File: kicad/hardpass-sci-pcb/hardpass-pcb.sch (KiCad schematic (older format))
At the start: 45 parts, among them IC1 APX803, P1 Pi_Zero, P2 OLED_I2C, P3 Pi_Zero, SW1 1, SW10 C/UP, SW11 0/OK, SW12 OK/DN, SW13 SHUTDN, SW2 2, SW3 3, SW4 4, SW5 5, SW6 6, SW7 7, SW8 8, SW9 9, U1 ISO7816, U2 ESP-12E, U3 SEC1210

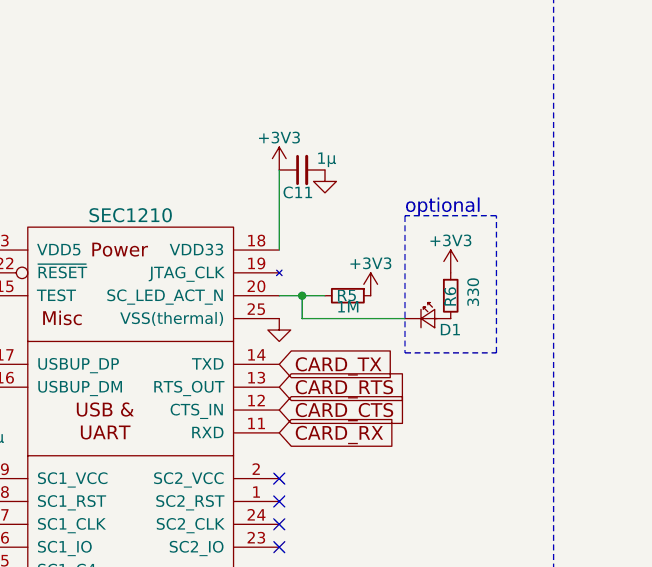
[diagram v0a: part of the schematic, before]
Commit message: small fixes
schematic: add either-or text to card-led
pcb: connect c10 to card-pin1
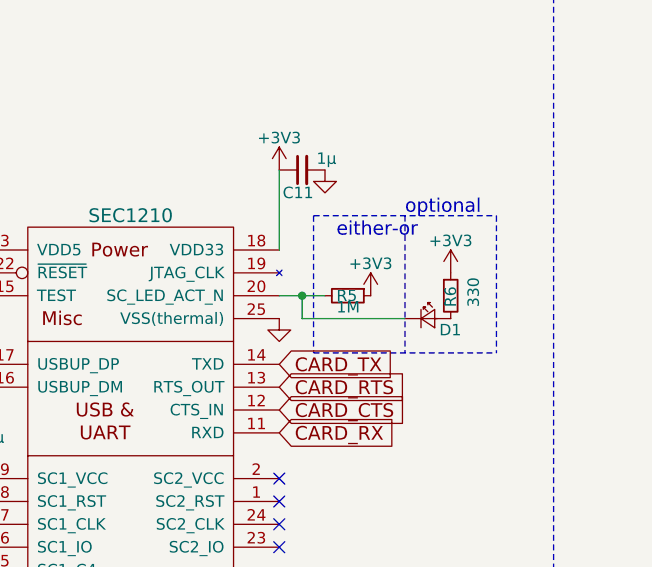
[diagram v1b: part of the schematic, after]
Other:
- note added: "either-or"
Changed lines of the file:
@@
 	10500 1600 10500 2200
 Wire Notes Line
-	10500 2200 10900 2200
+	10100 2200 10900 2200
 Wire Notes Line
-	10900 2200 10900 1600
+	10900 1600 10900 2200
 Wire Notes Line
-	10900 1600 10500 1600
+	10100 1600 10900 1600
 Text Notes 10500 1600 0    60   ~ 0
 optional
@@
 Text Notes 9300 3950 0    60   ~ 0
 CTS/RTS on the Pi: \nhttps://github.com/mholling/rpirtscts
+Wire Notes Line
+	10100 1600 10100 2200
+Text Notes 10200 1700 0    60   ~ 0
+either-or
 $EndSCHEMATC

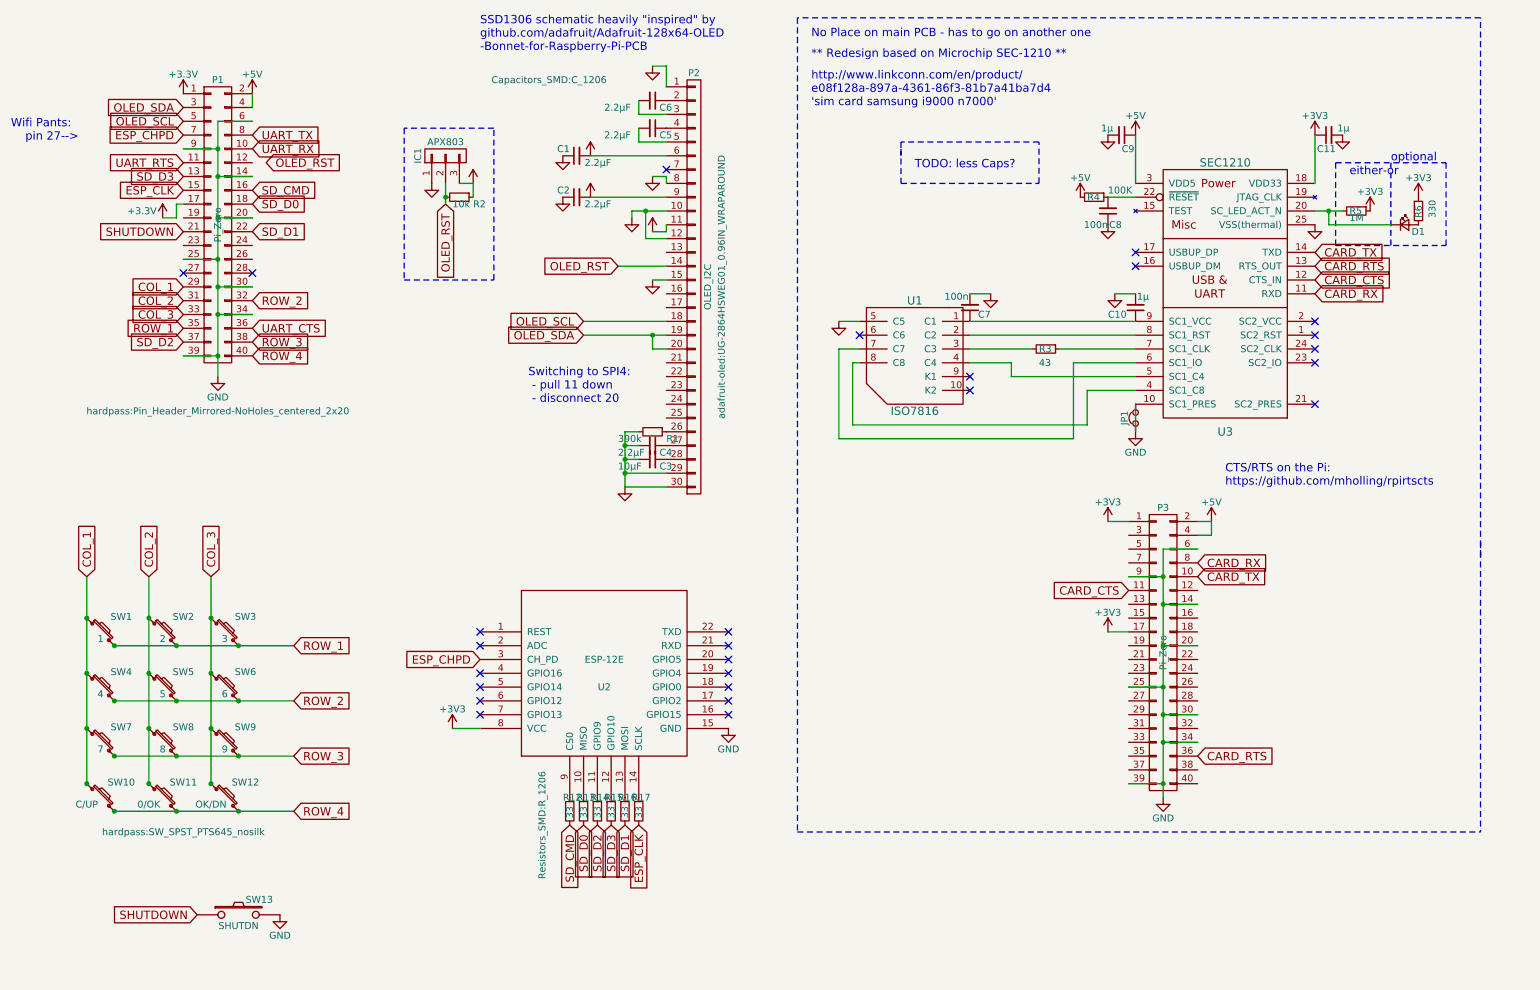
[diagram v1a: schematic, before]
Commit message: seperate hardpass and hardpass-sci kicad projects
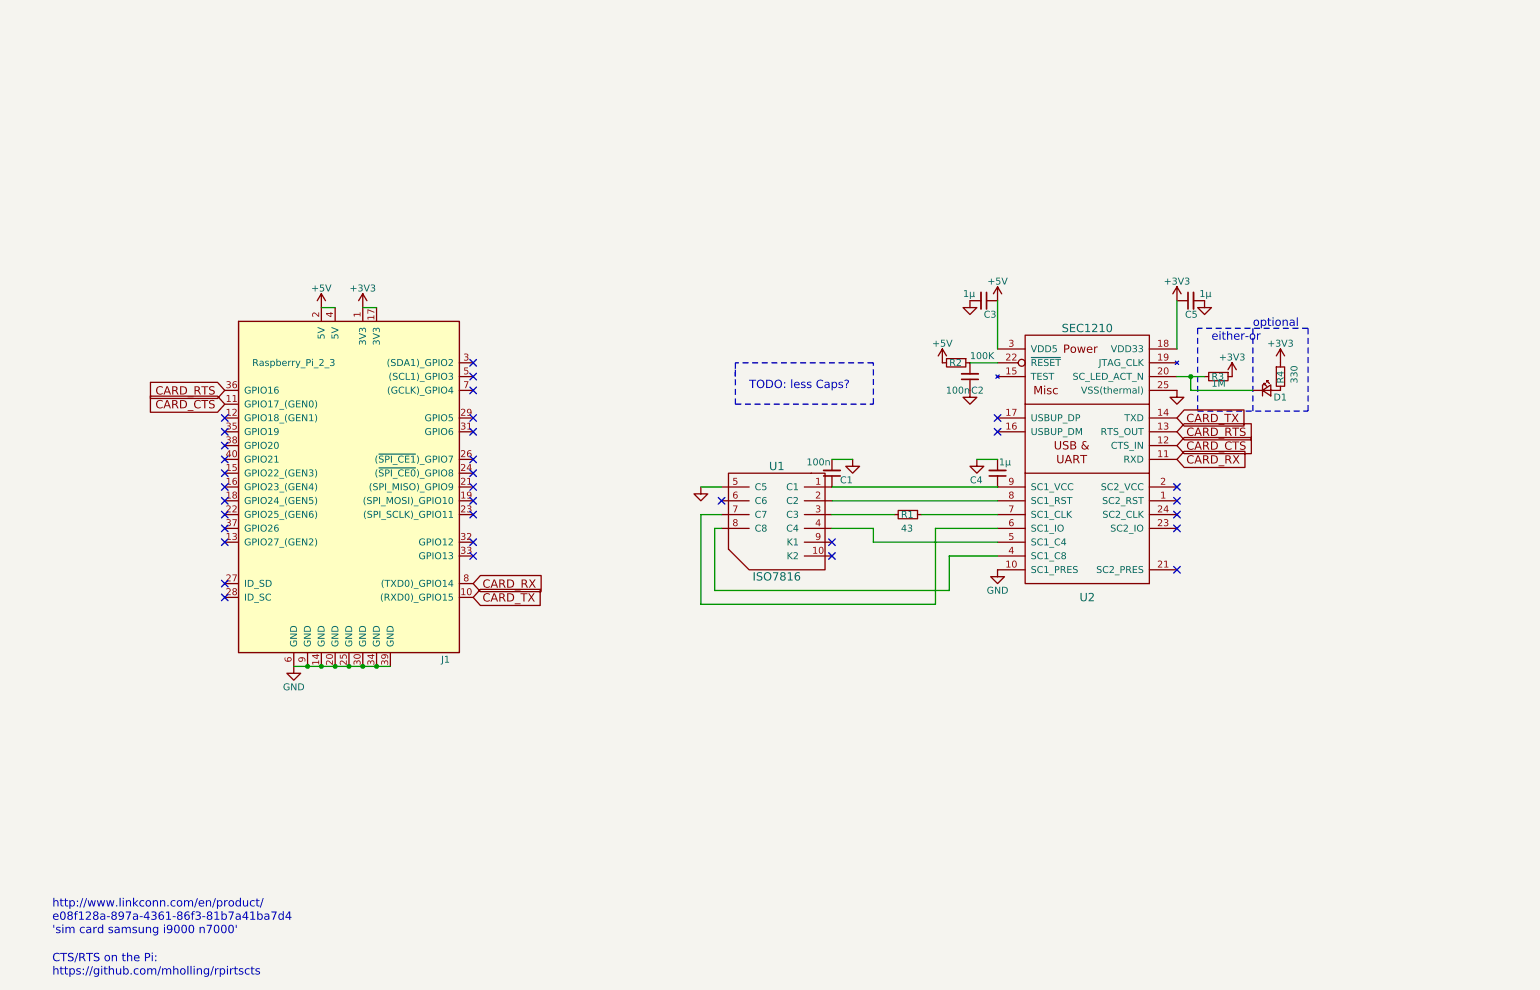
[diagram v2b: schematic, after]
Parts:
- removed C1, C2, C4, C5, C6: 2.2µF, Capacitors_SMD:C_1206, symbol C_Small
- removed C3: 10µF, Capacitors_SMD:C_1206, symbol C_Small
- removed IC1: APX803, TO_SOT_Packages_SMD:SOT-23, symbol CONN_01X03
- removed JP1: (no value), Resistors_SMD:R_0603, symbol Jumper_NC_Small
- removed P1: Pi_Zero, hardpass:Pin_Header_Mirrored-NoHoles_centered_2x20, symbol CONN_02X20
- removed P2: OLED_I2C, adafruit-oled:UG-2864HSWEG01_0.96IN_WRAPAROUND, symbol CONN_01X30
- removed P3: Pi_Zero, hardpass:Pin_Header_Straight_2x20_Pitch2.54mm_centered, symbol CONN_02X20
- removed R1: 390k, Resistors_SMD:R_1206, symbol R_Small
- removed R12, R13, R14, R15, R16, R17: 33, Resistors_SMD:R_1206, symbol R_Small
- removed R2: 10k, Resistors_SMD:R_1206, symbol R_Small
- removed SW1: 1, hardpass:SW_SPST_PTS645_nosilk, symbol SW_PUSH_SMALL
- removed SW10: C/UP, hardpass:SW_SPST_PTS645_nosilk, symbol SW_PUSH_SMALL
- removed SW11: 0/OK, hardpass:SW_SPST_PTS645_nosilk, symbol SW_PUSH_SMALL
- removed SW12: OK/DN, hardpass:SW_SPST_PTS645_nosilk, symbol SW_PUSH_SMALL
- removed SW13: SHUTDN, symbol SW_PUSH
- removed SW2: 2, hardpass:SW_SPST_PTS645_nosilk, symbol SW_PUSH_SMALL
- removed SW3: 3, hardpass:SW_SPST_PTS645_nosilk, symbol SW_PUSH_SMALL
- removed SW4: 4, hardpass:SW_SPST_PTS645_nosilk, symbol SW_PUSH_SMALL
- removed SW5: 5, hardpass:SW_SPST_PTS645_nosilk, symbol SW_PUSH_SMALL
- removed SW6: 6, hardpass:SW_SPST_PTS645_nosilk, symbol SW_PUSH_SMALL
- removed SW7: 7, hardpass:SW_SPST_PTS645_nosilk, symbol SW_PUSH_SMALL
- removed SW8: 8, hardpass:SW_SPST_PTS645_nosilk, symbol SW_PUSH_SMALL
- removed SW9: 9, hardpass:SW_SPST_PTS645_nosilk, symbol SW_PUSH_SMALL
- removed U2: ESP-12E, hardpass:ESP-12E_smd, symbol ESP-12E
- added J1: Raspberry_Pi_2_3, Pin_Headers:Pin_Header_Straight_2x20, symbol Raspberry_Pi_2_3
- renumbered C7 to C1, C8 to C2, C9 to C3, C10 to C4, C11 to C5, R3 to R1, R4 to R2, R5 to R3, R6 to R4, U3 to U2
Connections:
- net +3V3: now also J1.1 (3V3), J1.17 (3V3)
- net +5V: now also J1.2 (5V), J1.4 (5V)
- net CARD_CTS: now also J1.11 (GPIO17_(GEN0))
- net CARD_RTS: now also J1.36 (GPIO16)
- net CARD_RX: now also J1.8 ((TXD0)_GPIO14)
- net CARD_TX: now also J1.10 ((RXD0)_GPIO15)
- net GND: now also J1.14 (GND), J1.20 (GND), J1.25 (GND), J1.30 (GND), J1.34 (GND), J1.39 (GND), J1.6 (GND), J1.9 (GND)
- no-connect marks 26 -> 34
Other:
- note removed: "** Redesign based on Microchip SEC-1210 **"
- note removed: "No Place on main PCB - has to go on another one"
- note removed: "SSD1306 schematic heavily "inspired" by\ngithub.com/adafruit/Adafruit-128x64-OLED\n-Bonnet-for-Raspberry-Pi-PCB"
- note removed: "Switching to SPI4:\n - pull 11 down\n - disconnect 20"
- note removed: "Wifi Pants: \n pin 27-->"
- moved on the sheet: C1, C2, C3, C4, C5, D1, R1, R2, R3, R4, U1, U2

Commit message: change sec1210 footprint to handsoldering
should ease qfn soldering by hand due to the elongated pads. this also
required moveing some traces out of the way on the pcb.
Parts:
- U2: footprint Housings_DFN_QFN:QFN-24-1EP_5x5mm_Pitch0.65mm -> Housings_DFN_QFN:QFN-24-1EP_5x5mm_Pitch0.65mm_HandSoldering
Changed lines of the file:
@@
 F 0 "U2" H 8300 2750 60  0000 C CNN
 F 1 "SEC1210" H 8300 4700 60  0000 C CNN
-F 2 "Housings_DFN_QFN:QFN-24-1EP_5x5mm_Pitch0.65mm" H 8300 3600 60  0001 C CNN
+F 2 "Housings_DFN_QFN:QFN-24-1EP_5x5mm_Pitch0.65mm_HandSoldering" H 8300 3600 60  0001 C CNN
 F 3 "" H 8300 3600 60  0001 C CNN
 	1    8300 3750
